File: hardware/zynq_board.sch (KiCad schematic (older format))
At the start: 0 parts

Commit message: Triggerbus WIP.
Also added more production data
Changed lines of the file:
@@
 LIBS:sn74axc8t245
 LIBS:sn74lvc2t45
+LIBS:dmf05lcflp
+LIBS:txs02612
+LIBS:bss138ps
 LIBS:zynq_board-cache
 EELAYER 25 0
@@
 $EndSheet
 Wire Notes Line
-	7250 5350 7250 19950
+	7250 3800 7250 19950
 Wire Notes Line
 	7250 19950 13450 19950
 Wire Notes Line
-	13450 18400 13450 3800
+	13450 19950 13450 3800
 Wire Wire Line
 	13250 16050 19700 16050

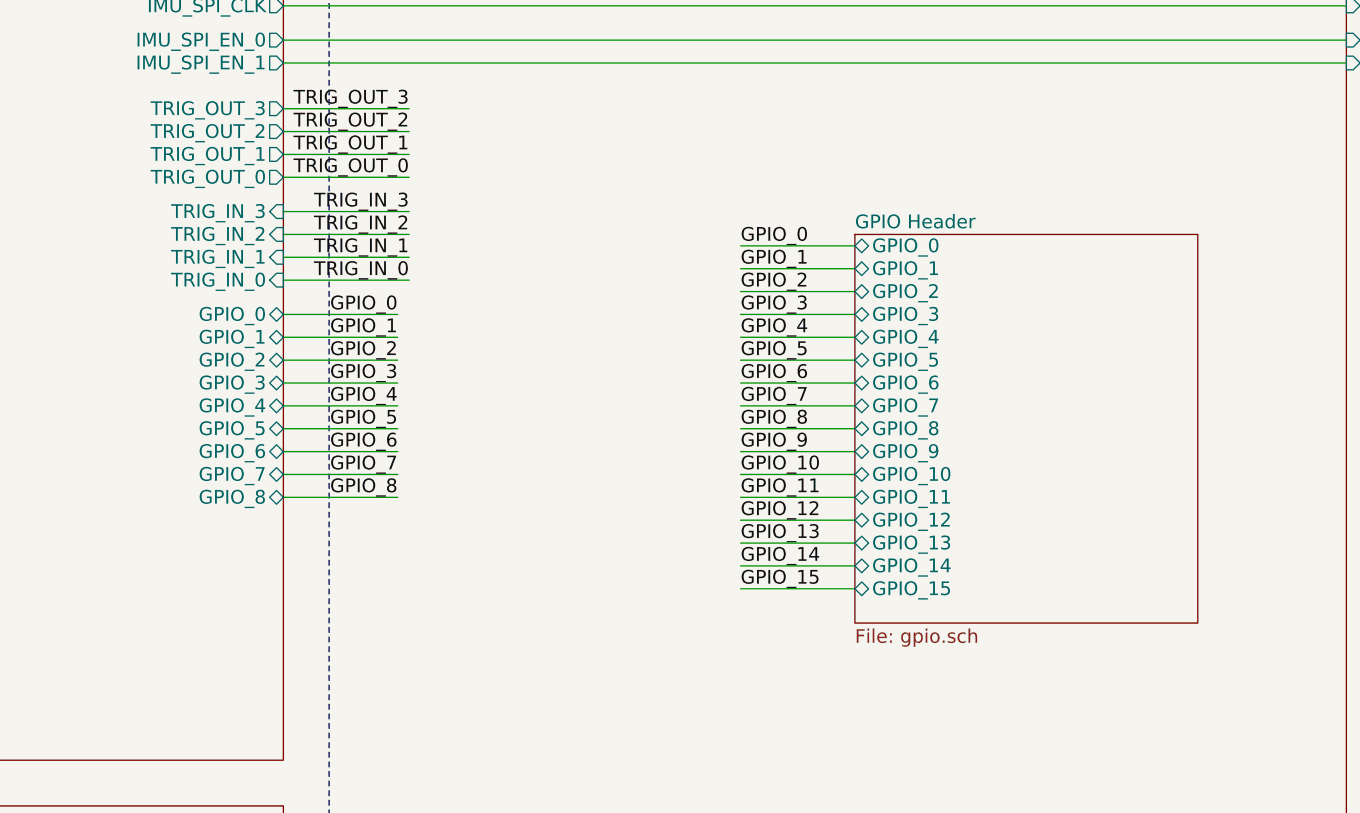
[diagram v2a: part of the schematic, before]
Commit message: Added Reset Button, Power LED, 2 Status LEDs and an external Button.
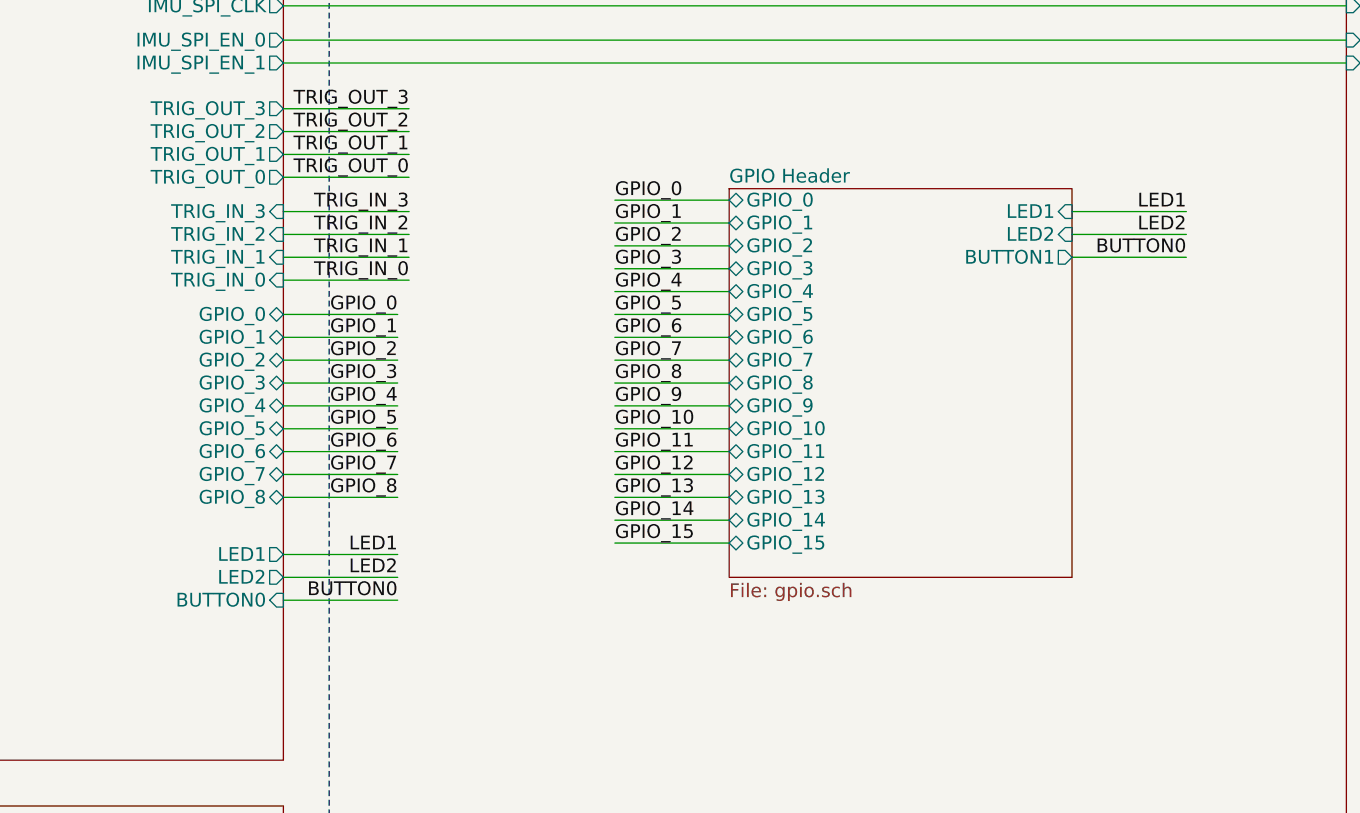
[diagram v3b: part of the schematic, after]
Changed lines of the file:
@@
 LIBS:bss138ps
 LIBS:max14854
+LIBS:switches
 LIBS:zynq_board-cache
 EELAYER 25 0
@@
 F37 "GPIO_7" B R 13250 10800 60
 F38 "GPIO_8" B R 13250 10900 60
+F39 "LED1" O R 13250 11150 60
+F40 "LED2" O R 13250 11250 60
+F41 "BUTTON0" I R 13250 11350 60
 $EndSheet
 $Sheet
@@
 	13250 10900 13750 10900
 $Sheet
-S 15750 9750 1500 1700
+S 15200 9550 1500 1700
 U 5B0F4BF9
 F0 "GPIO Header" 60
 F1 "gpio.sch" 60
-F2 "GPIO_0" B L 15750 9800 60
-F3 "GPIO_1" B L 15750 9900 60
-F4 "GPIO_2" B L 15750 10000 60
-F5 "GPIO_3" B L 15750 10100 60
-F6 "GPIO_4" B L 15750 10200 60
-F7 "GPIO_5" B L 15750 10300 60
-F8 "GPIO_6" B L 15750 10400 60
-F9 "GPIO_7" B L 15750 10500 60
-F10 "GPIO_8" B L 15750 10600 60
-F11 "GPIO_9" B L 15750 10700 60
-F12 "GPIO_10" B L 15750 10800 60
-F13 "GPIO_11" B L 15750 10900 60
-F14 "GPIO_12" B L 15750 11000 60
-F15 "GPIO_13" B L 15750 11100 60
-F16 "GPIO_14" B L 15750 11200 60
-F17 "GPIO_15" B L 15750 11300 60
-$EndSheet
-Text Label 15250 9800 0    60   ~ 0
+F2 "GPIO_0" B L 15200 9600 60
+F3 "GPIO_1" B L 15200 9700 60
+F4 "GPIO_2" B L 15200 9800 60
+F5 "GPIO_3" B L 15200 9900 60
+F6 "GPIO_4" B L 15200 10000 60
+F7 "GPIO_5" B L 15200 10100 60
+F8 "GPIO_6" B L 15200 10200 60
+F9 "GPIO_7" B L 15200 10300 60
+F10 "GPIO_8" B L 15200 10400 60
+F11 "GPIO_9" B L 15200 10500 60
+F12 "GPIO_10" B L 15200 10600 60
+F13 "GPIO_11" B L 15200 10700 60
+F14 "GPIO_12" B L 15200 10800 60
+F15 "GPIO_13" B L 15200 10900 60
+F16 "GPIO_14" B L 15200 11000 60
+F17 "GPIO_15" B L 15200 11100 60
+F18 "LED1" I R 16700 9650 60
+F19 "LED2" I R 16700 9750 60
+F20 "BUTTON1" O R 16700 9850 60
+$EndSheet
+Text Label 14700 9600 0    60   ~ 0
 GPIO_0
 Wire Wire Line
-	15250 9800 15750 9800
-Text Label 15250 9900 0    60   ~ 0
+	14700 9600 15200 9600
+Text Label 14700 9700 0    60   ~ 0
 GPIO_1
 Wire Wire Line
-	15250 9900 15750 9900
-Text Label 15250 10000 0    60   ~ 0
+	14700 9700 15200 9700
+Text Label 14700 9800 0    60   ~ 0
 GPIO_2
 Wire Wire Line
-	15250 10000 15750 10000
-Text Label 15250 10100 0    60   ~ 0
+	14700 9800 15200 9800
+Text Label 14700 9900 0    60   ~ 0
 GPIO_3
 Wire Wire Line
-	15250 10100 15750 10100
-Text Label 15250 10200 0    60   ~ 0
+	14700 9900 15200 9900
+Text Label 14700 10000 0    60   ~ 0
 GPIO_4
 Wire Wire Line
-	15250 10200 15750 10200
-Text Label 15250 10300 0    60   ~ 0
+	14700 10000 15200 10000
+Text Label 14700 10100 0    60   ~ 0
 GPIO_5
 Wire Wire Line
-	15250 10300 15750 10300
-Text Label 15250 10400 0    60   ~ 0
+	14700 10100 15200 10100
+Text Label 14700 10200 0    60   ~ 0
 GPIO_6
 Wire Wire Line
-	15250 10400 15750 10400
-Text Label 15250 10500 0    60   ~ 0
+	14700 10200 15200 10200
+Text Label 14700 10300 0    60   ~ 0
 GPIO_7
 Wire Wire Line
-	15250 10500 15750 10500
-Text Label 15250 10600 0    60   ~ 0
+	14700 10300 15200 10300
+Text Label 14700 10400 0    60   ~ 0
 GPIO_8
 Wire Wire Line
-	15250 10600 15750 10600
-Text Label 15250 10700 0    60   ~ 0
+	14700 10400 15200 10400
+Text Label 14700 10500 0    60   ~ 0
 GPIO_9
 Wire Wire Line
-	15250 10700 15750 10700
-Text Label 15250 10800 0    60   ~ 0
+	14700 10500 15200 10500
+Text Label 14700 10600 0    60   ~ 0
 GPIO_10
 Wire Wire Line
-	15250 10800 15750 10800
-Text Label 15250 10900 0    60   ~ 0
+	14700 10600 15200 10600
+Text Label 14700 10700 0    60   ~ 0
 GPIO_11
 Wire Wire Line
-	15250 10900 15750 10900
-Text Label 15250 11000 0    60   ~ 0
+	14700 10700 15200 10700
+Text Label 14700 10800 0    60   ~ 0
 GPIO_12
 Wire Wire Line
-	15250 11000 15750 11000
-Text Label 15250 11100 0    60   ~ 0
+	14700 10800 15200 10800
+Text Label 14700 10900 0    60   ~ 0
 GPIO_13
 Wire Wire Line
-	15250 11100 15750 11100
-Text Label 15250 11200 0    60   ~ 0
+	14700 10900 15200 10900
+Text Label 14700 11000 0    60   ~ 0
 GPIO_14
 Wire Wire Line
-	15250 11200 15750 11200
-Text Label 15250 11300 0    60   ~ 0
+	14700 11000 15200 11000
+Text Label 14700 11100 0    60   ~ 0
 GPIO_15
 Wire Wire Line
-	15250 11300 15750 11300
+	14700 11100 15200 11100
+Text Label 13750 11150 2    60   ~ 0
+LED1
+Text Label 13750 11250 2    60   ~ 0
+LED2
+Text Label 13750 11350 2    60   ~ 0
+BUTTON0
+Wire Wire Line
+	13250 11150 13750 11150
+Wire Wire Line
+	13250 11250 13750 11250
+Wire Wire Line
+	13250 11350 13750 11350
+Text Label 17200 9650 2    60   ~ 0
+LED1
+Text Label 17200 9750 2    60   ~ 0
+LED2
+Text Label 17200 9850 2    60   ~ 0
+BUTTON0
+Wire Wire Line
+	16700 9650 17200 9650
+Wire Wire Line
+	16700 9750 17200 9750
+Wire Wire Line
+	16700 9850 17200 9850
 $EndSCHEMATC

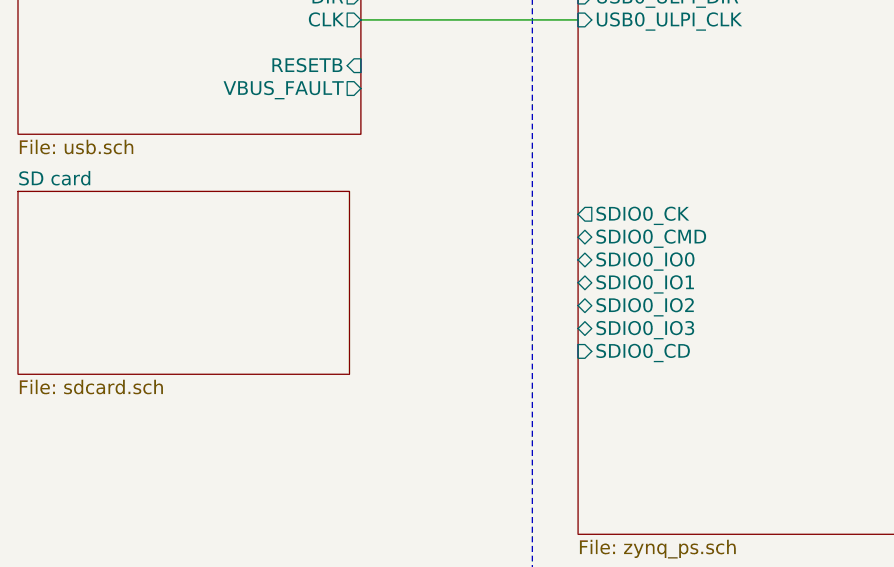
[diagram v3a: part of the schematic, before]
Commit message: Added Sdcard Slot.
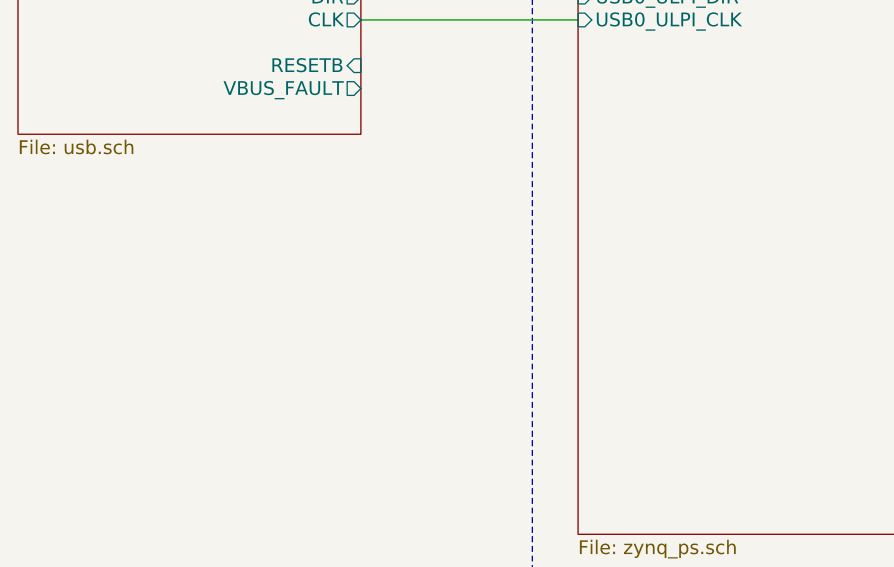
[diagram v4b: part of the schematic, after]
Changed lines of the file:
@@
 $Descr A1 33110 23386
 encoding utf-8
-Sheet 1 21
+Sheet 1 20
 Title ""
 Date ""
@@
 F0 "Memory" 60
 F1 "zynq_memory.sch" 60
-$EndSheet
-$Sheet
-S 7450 8450 2750 3550
-U 596E7567
-F0 "Processing System IO" 60
-F1 "zynq_ps.sch" 60
-F2 "SDIO0_CK" O L 7450 10600 60
-F3 "SDIO0_CMD" B L 7450 10700 60
-F4 "SDIO0_IO0" B L 7450 10800 60
-F5 "SDIO0_IO1" B L 7450 10900 60
-F6 "SDIO0_IO2" B L 7450 11000 60
-F7 "SDIO0_IO3" B L 7450 11100 60
-F8 "SDIO0_CD" I L 7450 11200 60
-F9 "USB0_ULPI_DATA0" B L 7450 9250 60
-F10 "USB0_ULPI_DATA1" B L 7450 9150 60
-F11 "USB0_ULPI_DATA2" B L 7450 9050 60
-F12 "USB0_ULPI_DATA3" B L 7450 8950 60
-F13 "USB0_ULPI_DATA5" B L 7450 8750 60
-F14 "USB0_ULPI_DATA6" B L 7450 8650 60
-F15 "USB0_ULPI_DATA7" B L 7450 8550 60
-F16 "USB0_ULPI_DATA4" B L 7450 8850 60
-F17 "USB0_ULPI_CLK" I L 7450 9750 60
-F18 "USB0_ULPI_DIR" I L 7450 9650 60
-F19 "USB0_ULPI_STP" O L 7450 9450 60
-F20 "USB0_ULPI_NXT" I L 7450 9550 60
 $EndSheet
 $Sheet
@@
 Text Notes 5450 6200 0    60   ~ 0
 TPS65911 ?
-$Sheet
-S 5000 10500 1450 800
-U 5A99EB39
-F0 "SD card" 60
-F1 "sdcard.sch" 60
-$EndSheet
 $Sheet
 S 10500 17900 2750 2500
@@
 Wire Wire Line
 	16700 9850 17200 9850
+$Sheet
+S 7450 8450 2750 3550
+U 596E7567
+F0 "Processing System IO" 60
+F1 "zynq_ps.sch" 60
+F2 "USB0_ULPI_DATA0" B L 7450 9250 60
+F3 "USB0_ULPI_DATA1" B L 7450 9150 60
+F4 "USB0_ULPI_DATA2" B L 7450 9050 60
+F5 "USB0_ULPI_DATA3" B L 7450 8950 60
+F6 "USB0_ULPI_DATA5" B L 7450 8750 60
+F7 "USB0_ULPI_DATA6" B L 7450 8650 60
+F8 "USB0_ULPI_DATA7" B L 7450 8550 60
+F9 "USB0_ULPI_DATA4" B L 7450 8850 60
+F10 "USB0_ULPI_CLK" I L 7450 9750 60
+F11 "USB0_ULPI_DIR" I L 7450 9650 60
+F12 "USB0_ULPI_STP" O L 7450 9450 60
+F13 "USB0_ULPI_NXT" I L 7450 9550 60
+$EndSheet
 $EndSCHEMATC

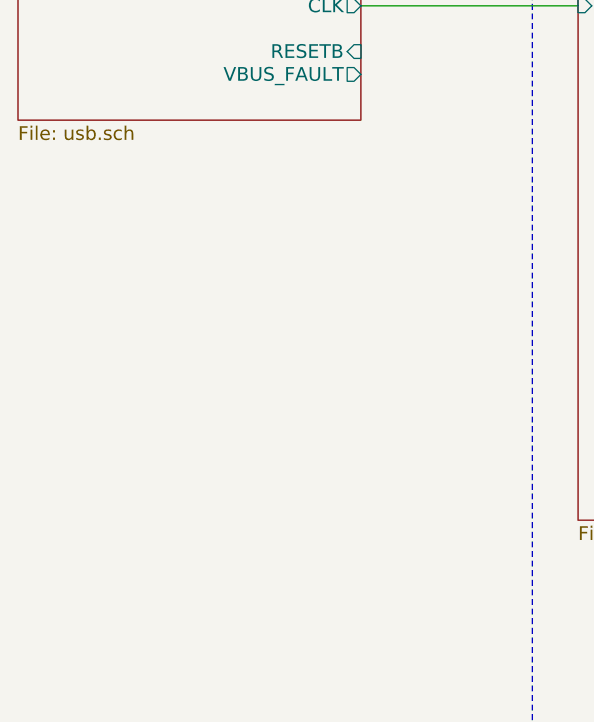
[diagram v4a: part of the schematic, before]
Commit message: Added USB-Uart subschematic. WIP
USB-Uart will be bus powered. Buffer between FTDI and FPGA is missing.
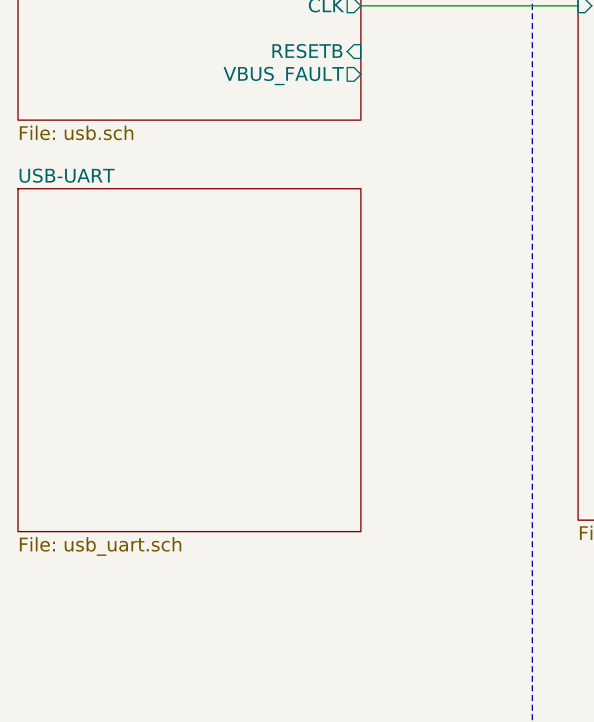
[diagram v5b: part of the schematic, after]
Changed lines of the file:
@@
 LIBS:max14854
 LIBS:switches
+LIBS:ft234xd
 LIBS:zynq_board-cache
 EELAYER 25 0
@@
 $Descr A1 33110 23386
 encoding utf-8
-Sheet 1 20
+Sheet 1 21
 Title ""
 Date ""
@@
 F13 "USB0_ULPI_NXT" I L 7450 9550 60
 $EndSheet
+$Sheet
+S 5000 10550 1500 1500
+U 5AD932C0
+F0 "USB-UART" 60
+F1 "usb_uart.sch" 60
+$EndSheet
 $EndSCHEMATC

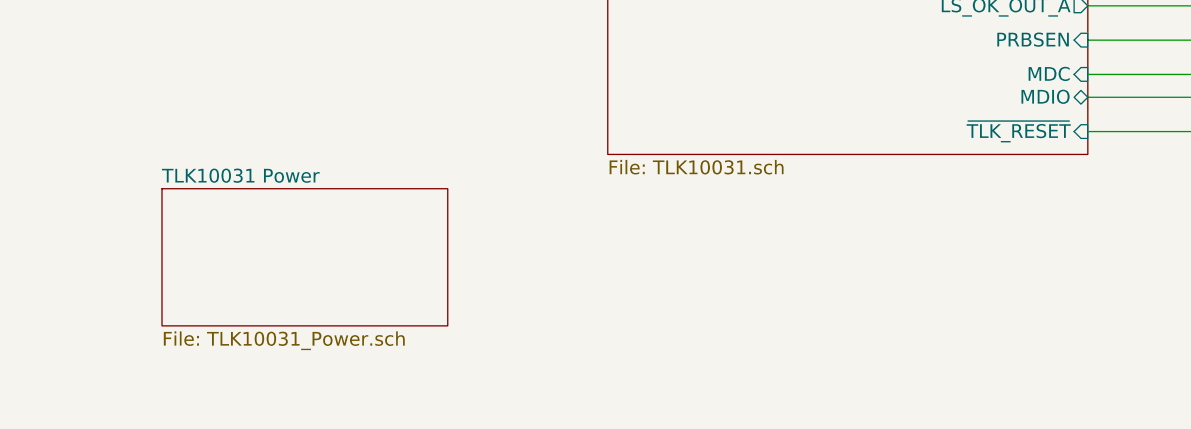
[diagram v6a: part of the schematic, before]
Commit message: Added decoupling Caps for TLK
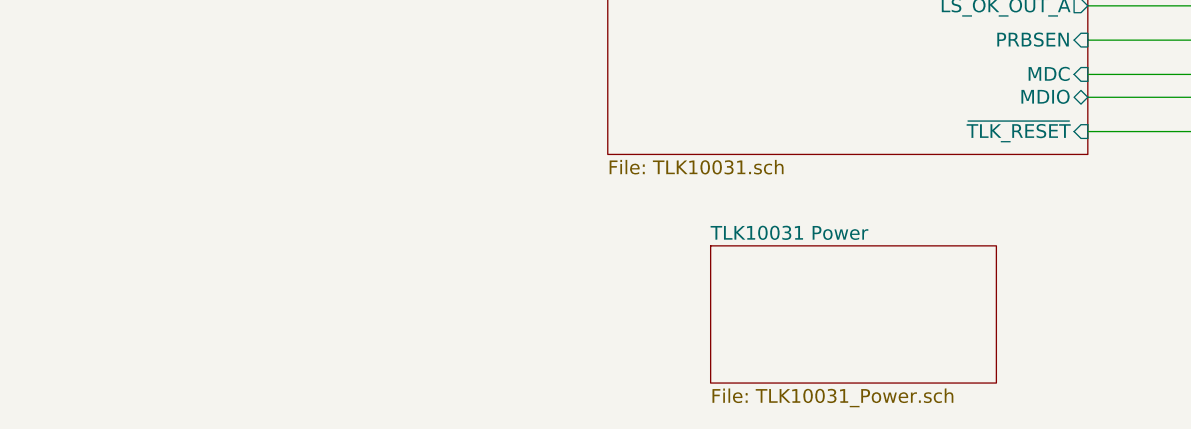
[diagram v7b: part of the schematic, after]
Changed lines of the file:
@@
 $EndSheet
 $Sheet
-S 18650 21150 1250 600
+S 21050 21400 1250 600
 U 5ACA2ECE
 F0 "TLK10031 Power" 60
